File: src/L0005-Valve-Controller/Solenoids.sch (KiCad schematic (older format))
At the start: 36 parts, among them K1 AQH0223AX, P3 647676-3

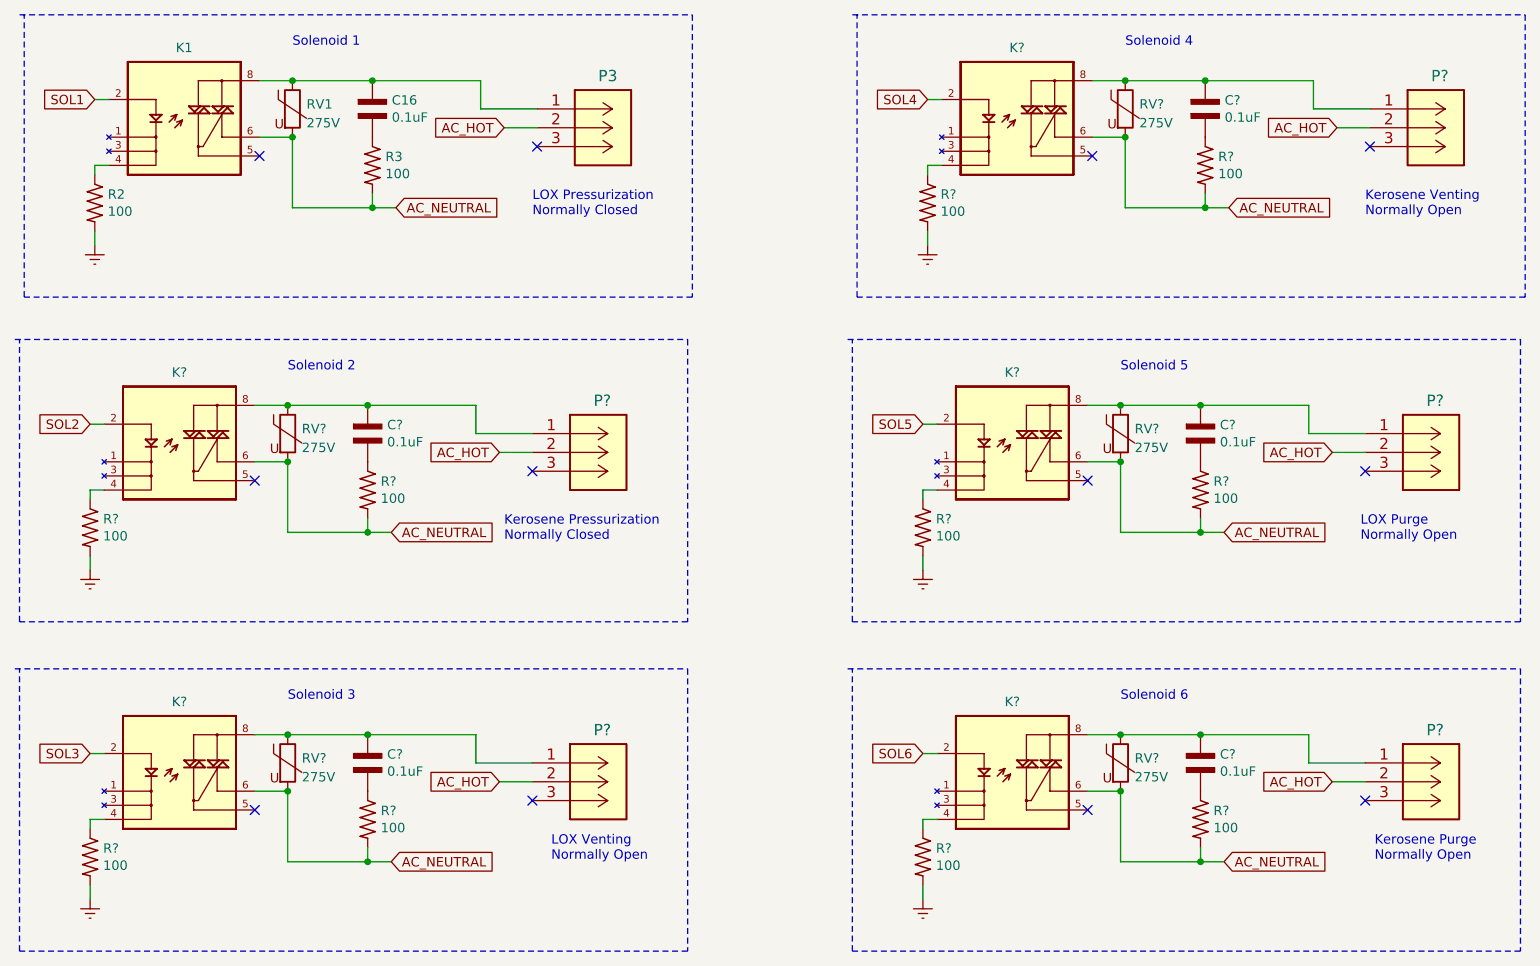
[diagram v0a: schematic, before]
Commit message: Added AC source to schematic
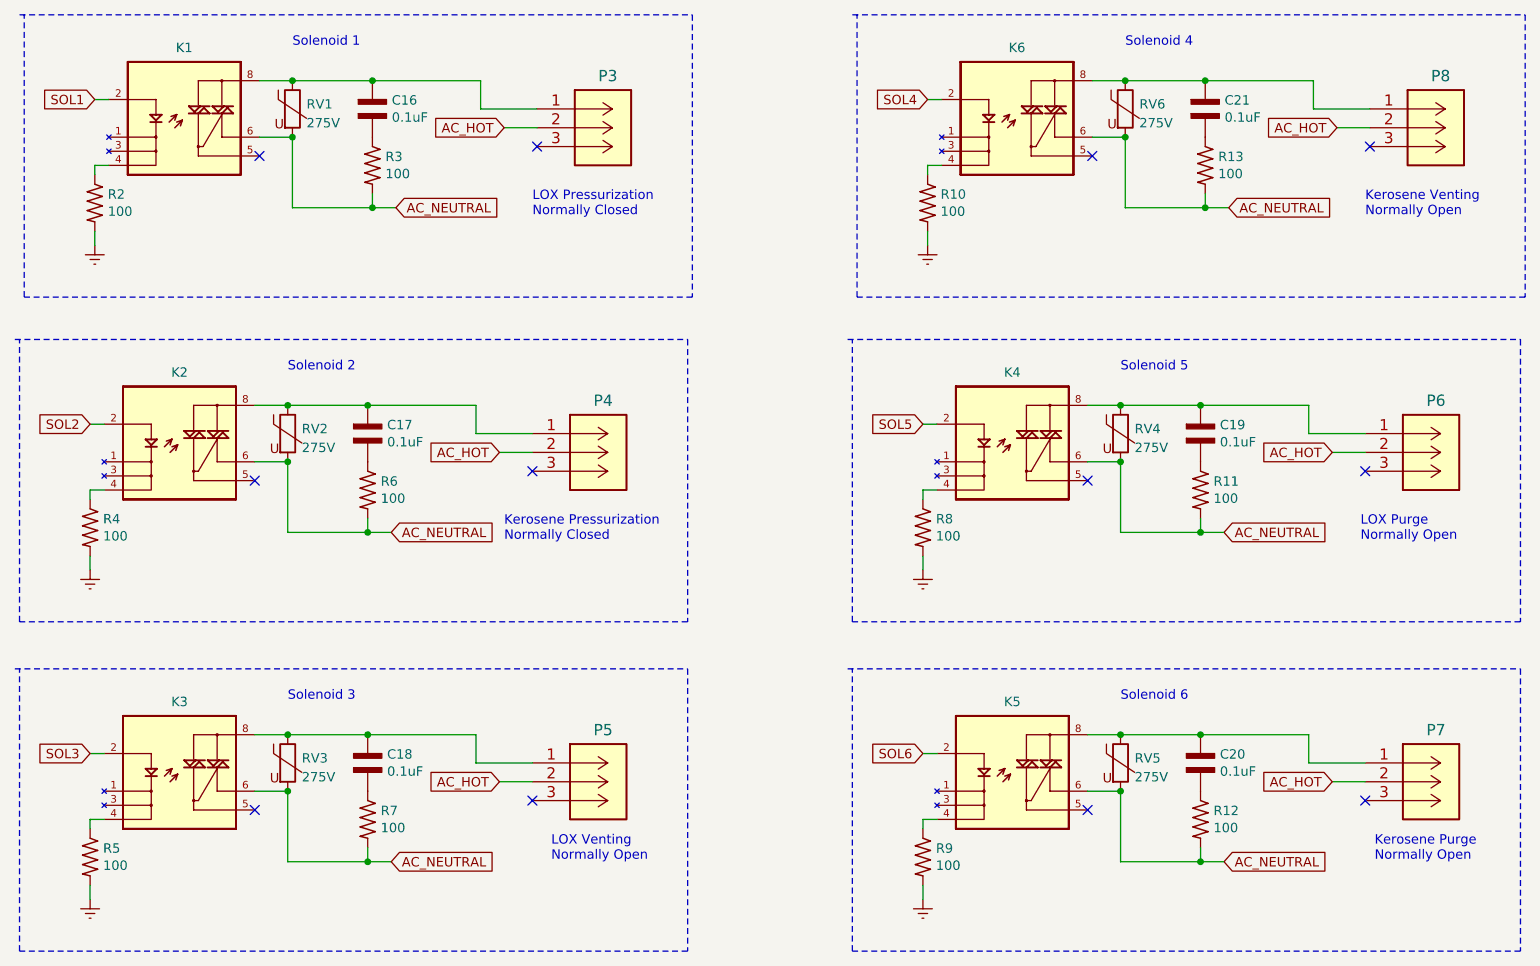
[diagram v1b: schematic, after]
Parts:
- gave numbers to parts that had none: 30
